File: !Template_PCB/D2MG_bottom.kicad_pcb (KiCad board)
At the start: 2 copper layers, 33 x 86.5 mm, 0 parts

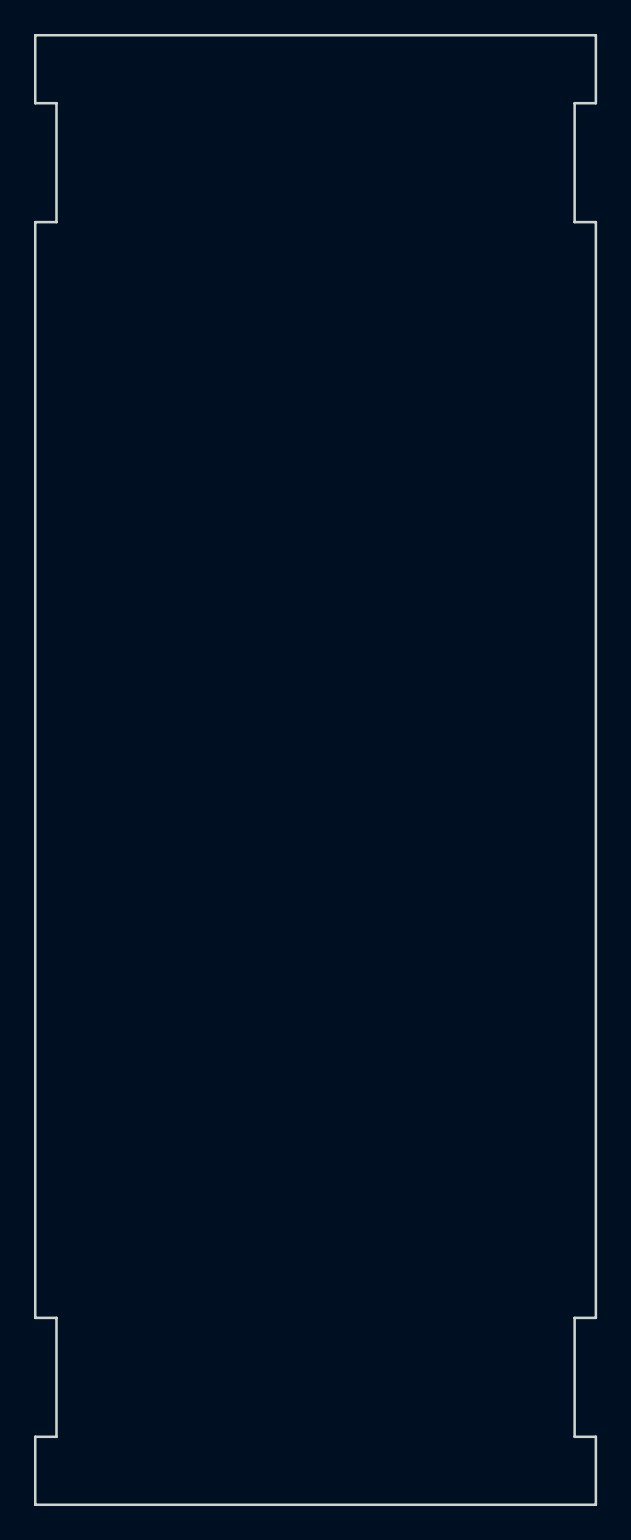
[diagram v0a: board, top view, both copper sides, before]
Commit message: + Spruce_60x70 Template_PCB
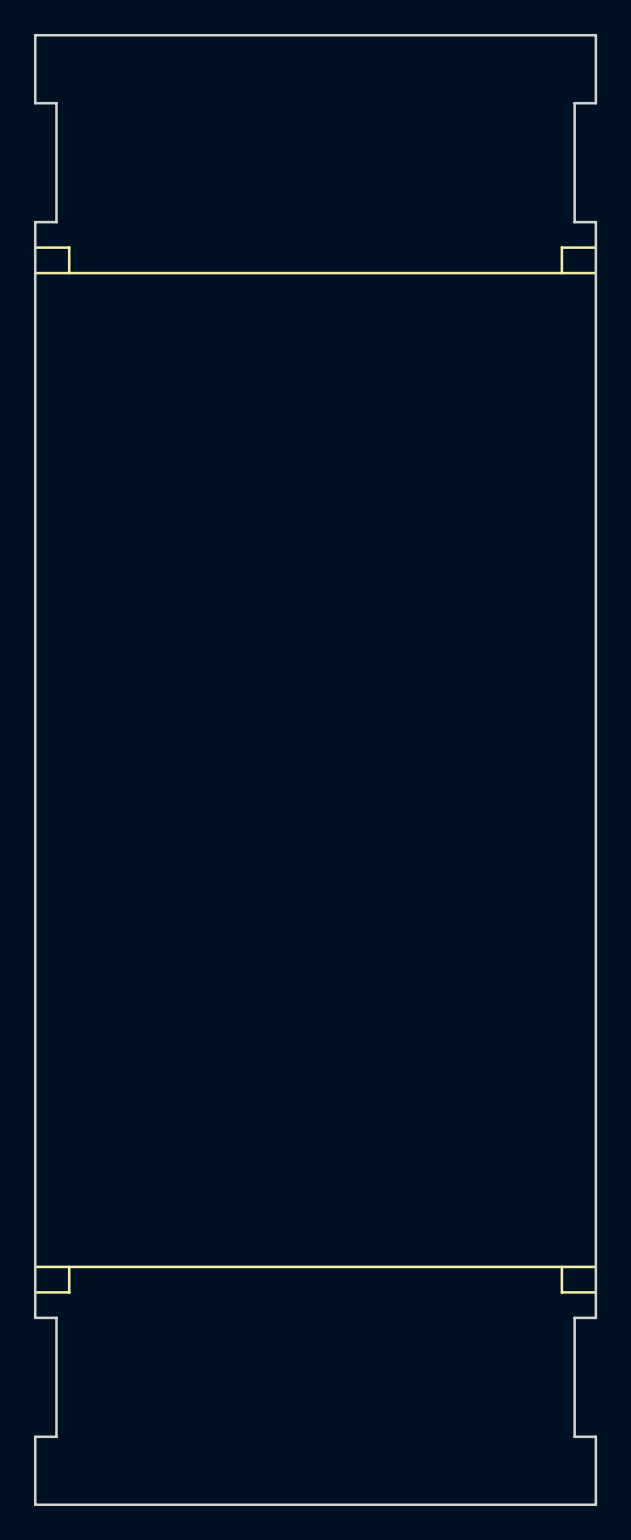
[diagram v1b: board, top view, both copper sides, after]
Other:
- board text removed: "bottom"
- board text removed: "top"
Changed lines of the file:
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@@
     (links 0)
     (no_connects 0)
-    (area 98.182142 48.424999 134.275001 138.075001)
+    (area 99.924999 49.924999 133.075001 136.575001)
     (thickness 1.6)
-    (drawings 35)
+    (drawings 33)
     (tracks 0)
     (zones 0)
@@
     (uvia_drill 0.3)
   )
-  (gr_text top (at 103.5 63) (layer Dwgs.User)
-    (effects (font (size 1.5 1.5) (thickness 0.3)))
-  )
-  (gr_text bottom (at 130.5 71 90) (layer Dwgs.User)
-    (effects (font (size 1.5 1.5) (thickness 0.3)))
-  )
-  (gr_line (start 102 62.5) (end 102 64) (angle 90) (layer Dwgs.User) (width 0.15))
-  (gr_line (start 100 62.5) (end 102 62.5) (angle 90) (layer Dwgs.User) (width 0.15))
-  (gr_line (start 131 62.5) (end 131 64) (angle 90) (layer Dwgs.User) (width 0.15))
-  (gr_line (start 133 62.5) (end 131 62.5) (angle 90) (layer Dwgs.User) (width 0.15))
-  (gr_line (start 131 124) (end 131 122.5) (angle 90) (layer Dwgs.User) (width 0.15))
-  (gr_line (start 133 124) (end 131 124) (angle 90) (layer Dwgs.User) (width 0.15))
-  (gr_line (start 102 124) (end 100 124) (angle 90) (layer Dwgs.User) (width 0.15))
-  (gr_line (start 102 122.5) (end 102 124) (angle 90) (layer Dwgs.User) (width 0.15))
-  (gr_line (start 101.5 50) (end 101.5 136.5) (angle 90) (layer Dwgs.User) (width 0.15))
-  (gr_line (start 131.5 136.5) (end 131.5 50) (angle 90) (layer Dwgs.User) (width 0.15))
+  (gr_line (start 102 62.5) (end 102 64) (angle 90) (layer F.SilkS) (width 0.15))
+  (gr_line (start 100 62.5) (end 102 62.5) (angle 90) (layer F.SilkS) (width 0.15))
+  (gr_line (start 131 62.5) (end 131 64) (angle 90) (layer F.SilkS) (width 0.15))
+  (gr_line (start 133 62.5) (end 131 62.5) (angle 90) (layer F.SilkS) (width 0.15))
+  (gr_line (start 131 124) (end 131 122.5) (angle 90) (layer F.SilkS) (width 0.15))
+  (gr_line (start 133 124) (end 131 124) (angle 90) (layer F.SilkS) (width 0.15))
+  (gr_line (start 102 124) (end 100 124) (angle 90) (layer F.SilkS) (width 0.15))
+  (gr_line (start 102 122.5) (end 102 124) (angle 90) (layer F.SilkS) (width 0.15))
+  (gr_line (start 101.5 50) (end 101.5 136.5) (angle 90) (layer B.SilkS) (width 0.15))
+  (gr_line (start 131.5 136.5) (end 131.5 50) (angle 90) (layer B.SilkS) (width 0.15))
   (gr_line (start 100 93.25) (end 133 93.25) (angle 90) (layer Dwgs.User) (width 0.15))
-  (gr_line (start 133 122.5) (end 100 122.5) (angle 90) (layer Dwgs.User) (width 0.15))
-  (gr_line (start 133 64) (end 100 64) (angle 90) (layer Dwgs.User) (width 0.15))
+  (gr_line (start 133 122.5) (end 100 122.5) (angle 90) (layer F.SilkS) (width 0.15))
+  (gr_line (start 133 64) (end 100 64) (angle 90) (layer F.SilkS) (width 0.15))
   (gr_line (start 133 54) (end 131.75 54) (angle 90) (layer Edge.Cuts) (width 0.15))
   (gr_line (start 131.75 54) (end 131.75 61) (angle 90) (layer Edge.Cuts) (width 0.15))

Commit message: .
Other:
- net class wide wide added: clearance 0.2, trace_width 1, via_dia 0.9, via_drill 0.4
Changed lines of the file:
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@@
+    (uvia_drill 0.3)
+  )
+  (net_class "wide wide" ""
+    (clearance 0.2)
+    (trace_width 1)
+    (via_dia 0.9)
+    (via_drill 0.4)
+    (uvia_dia 0.7)
     (uvia_drill 0.3)
   )
